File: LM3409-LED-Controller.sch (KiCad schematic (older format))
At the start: 24 parts, among them J1 PWM_IN, J2 IADJ, J3 BARREL_JACK, J4 LED+, J5 LED-, J6 EN, Q1 DMPH6050SK3, Q2 ZXMN7A11K, U1 LM3409HV-Q1

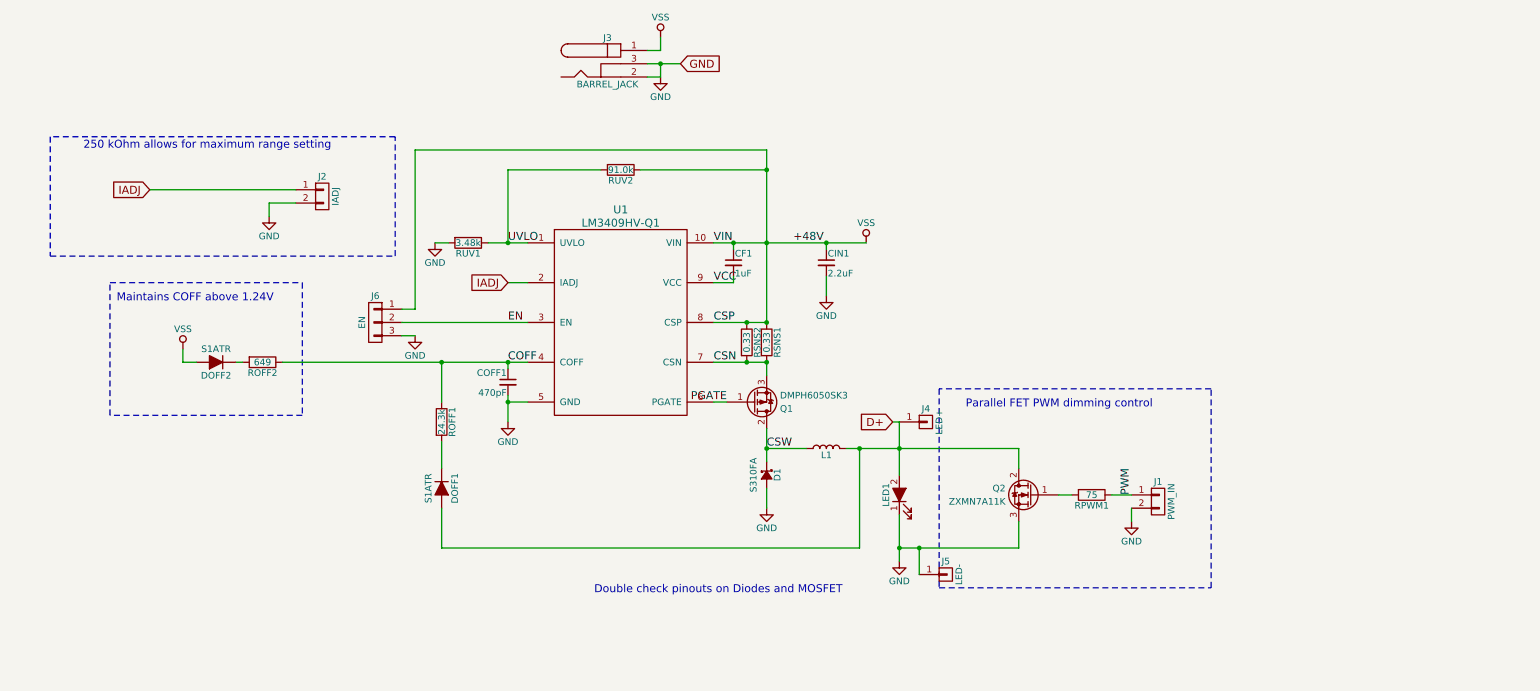
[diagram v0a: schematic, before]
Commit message: Replace parallel FET with CSD19538Q2 100-V, 49-mΩ NexFET. Added UCC27511 Gate Driver.
Redesign based on TI Designs: TIDA-01415.
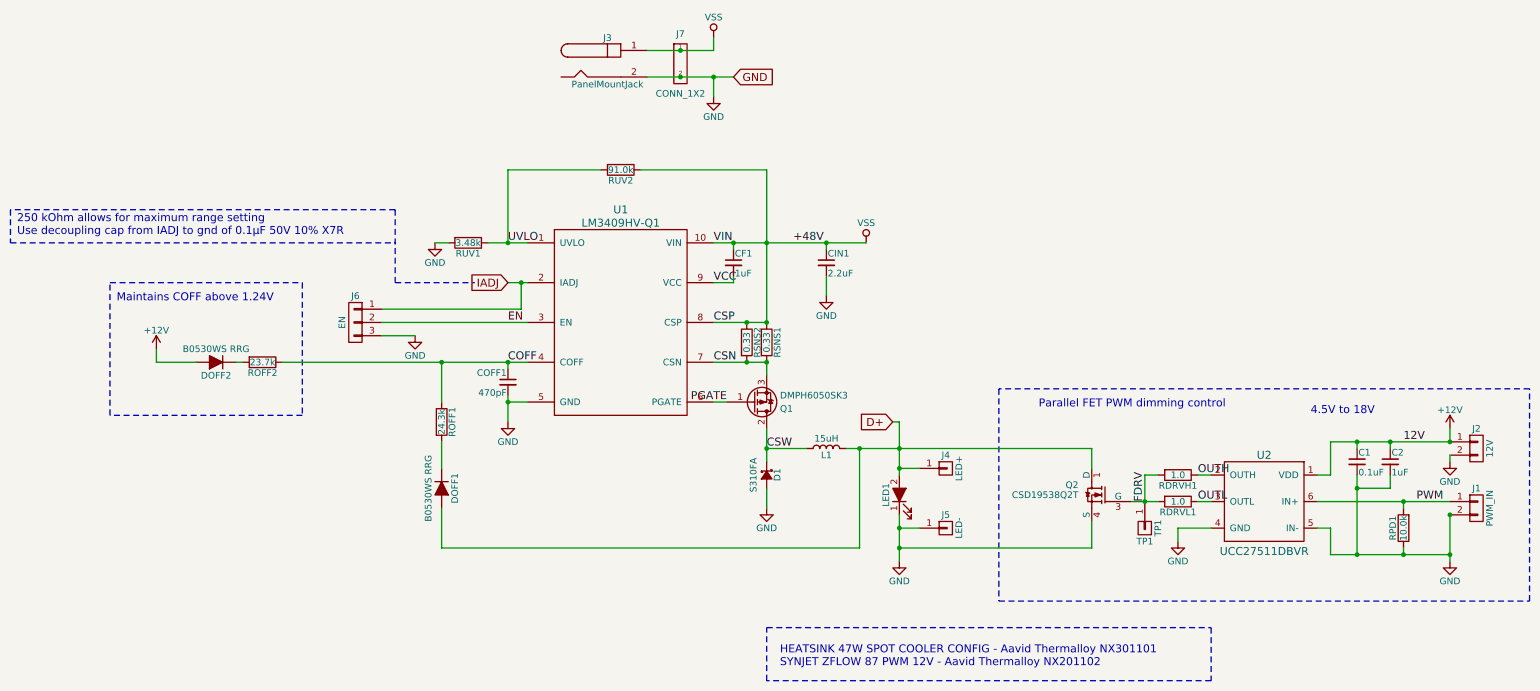
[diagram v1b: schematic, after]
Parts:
- removed J3: BARREL_JACK, Connectors:JACK_ALIM, symbol BARREL_JACK
- removed Q2: ZXMN7A11K, Project_Footprints:TO252_DPAK, symbol Q_NMOS_GDS
- removed RPWM1: 75, Resistors_SMD:R_0805, symbol R
- added C1: 0.1uF, Capacitors_SMD:C_0603, symbol C_Small
- added C2: 1uF, Capacitors_SMD:C_0805, symbol C_Small
- added J3: PanelMountJack, Project_Footprints:PanelMountJack_11mm, symbol PanelMountJack
- added J7: CONN_1X2, Wire_Connections_Bridges:WireConnection_2.00mmDrill, symbol CONN_1X2
- added Q2: CSD19538Q2T, Project_Footprints:SON_2mm_2mm_thermal, symbol CSD19538Q2T
- added RDRVH1, RDRVL1: 1.0, Resistors_SMD:R_0603, symbol R
- added RPD1: 10.0k, Resistors_SMD:R_0603, symbol R
- added TP1: TP1, Project_Footprints:Test_Point_1mm, symbol CONN_01X01
- added U2: UCC27511DBVR, Project_Footprints:SOT-23-1.75mm_3.0mm, symbol UCC27511DBVR
- CF1: footprint Capacitors_SMD:C_0603 -> Capacitors_SMD:C_0805; Description (none) -> CAP CER 1UF 50V X7R 0805
- CIN1: Description (none) -> CAP CER 2.2UF 100V X7R 1210; Part # (none) -> CL32B225KCJSNNE
- COFF1: Description (none) -> CAP CER 470PF 100V X7R 0402
- D1: Description (none) -> DIODE SCHOTTKY 100V 3A SOD123FA
- DOFF1, DOFF2: value S1ATR -> B0530WS RRG; footprint Project_Footprints:D_2026 -> Diodes_SMD:D_SOD-323F; Description (none) -> DIODE SCHOTTKY 30V 200MA SOD323F
- J2: value IADJ -> 12V
- L1: Description (none) -> FIXED IND 15UH 5A 27 MOHM SMD
- Q1: Description (none) -> MOSFET P-CH 60V 7.2A DPAK
- ROFF1: Description (none) -> RES SMD 24.3K OHM 1% 1/8W 0805
- ROFF2: value 649 -> 23.7k; Description (none) -> RES SMD 23.7K OHM 1% 1/8W 0805
- RSNS1, RSNS2: Description (none) -> RES 0.33 OHM 1% 1/2W 1206
- RUV1: Description (none) -> RES SMD 3.48K OHM 1% 1/8W 0805
- RUV2: Description (none) -> RES SMD 91K OHM 1% 1/8W 0805
- U1: Description (none) -> IC LED DRIVER CTRLR DIM 10MSOP
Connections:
- net D+: now also Q2.1 (D), Q2.2 (D), Q2.5 (D), Q2.6 (D), Q2.8 (D)
- net GND: now also C1.2, C2.2, J3.2, J7.2, Q2.4 (S), Q2.7 (S), RPD1.1, U2.4 (GND), U2.5 (IN-)
- net IADJ: now also J6.1 (P1); no longer J2.1 (P1)
- net PWM: now also RPD1.2, U2.6 (IN+)
- net VSS: now also J3.1, J7.1; no longer DOFF2.2 (A), J6.1 (P1)
- new net +12V: C1.1, C2.1, DOFF2.2 (A), J2.1 (P1), U2.1 (VDD)
- new net FDRV: Q2.3 (G), RDRVH1.2, RDRVL1.2, TP1.1 (P1)
- new net OUTH: RDRVH1.1, U2.2 (OUTH)
- new net OUTL: RDRVL1.1, U2.3 (OUTL)
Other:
- note added: "250 kOhm allows for maximum range setting\nUse decoupling cap from IADJ to gnd of 0.1µF 50V 10% X7R"
- note added: "4.5V to 18V"
- note added: "HEATSINK 47W SPOT COOLER CONFIG - Aavid Thermalloy NX301101\nSYNJET ZFLOW 87 PWM 12V - Aavid Thermalloy NX201102\n"
- note removed: "250 kOhm allows for maximum range setting"
- note removed: "Double check pinouts on Diodes and MOSFET"
- moved on the sheet: J1, J4, J5, J6

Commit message: Changed secondary voltage input to 9V
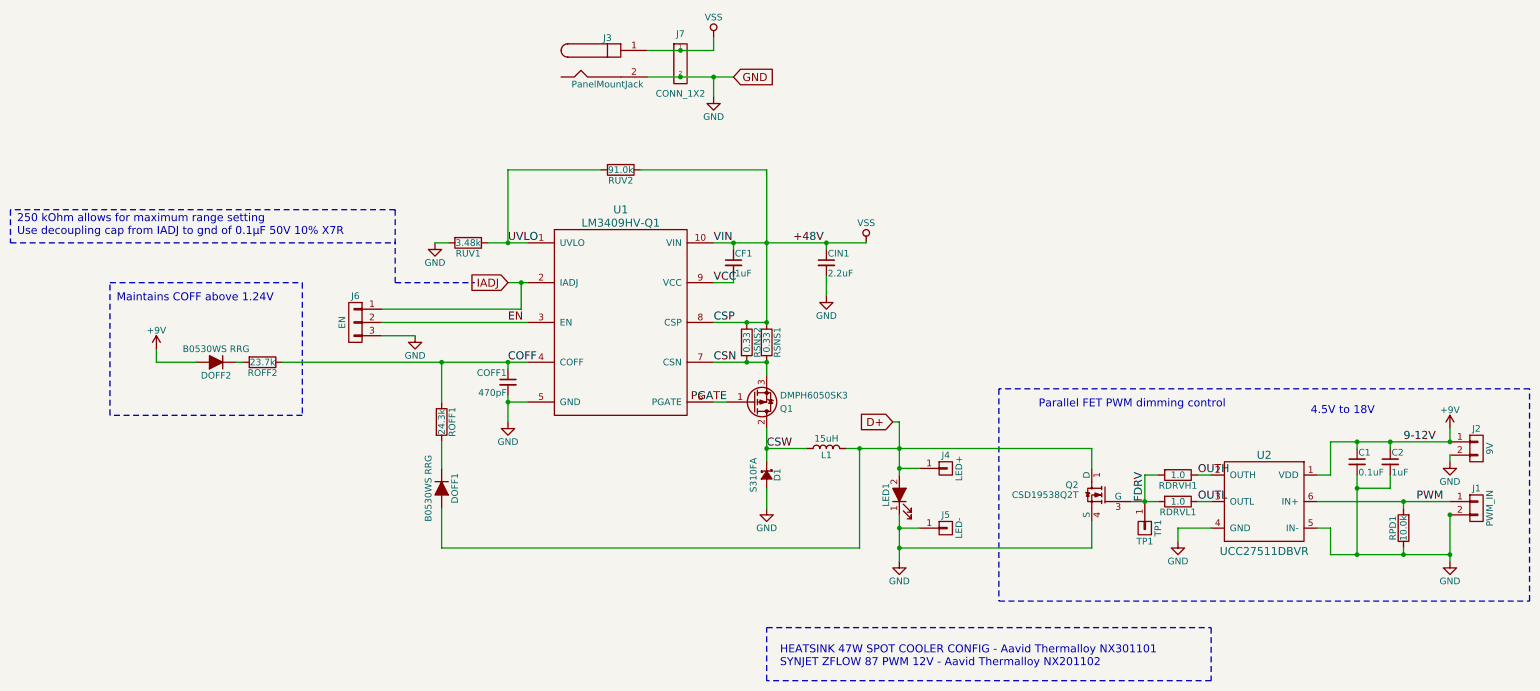
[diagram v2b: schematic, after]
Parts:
- J2: value 12V -> 9V
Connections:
- net +12V renamed +9V
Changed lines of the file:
@@
 	10650 5450 10650 5650
 Connection ~ 11200 5650
-$Comp
-L +12V #PWR012
-U 1 1 5A34D57E
-P 11550 4700
-F 0 "#PWR012" H 11550 4550 50  0001 C CNN
-F 1 "+12V" H 11550 4840 50  0000 C CNN
-F 2 "" H 11550 4700 50  0001 C CNN
-F 3 "" H 11550 4700 50  0001 C CNN
-	1    11550 4700
-	1    0    0    -1
-$EndComp
 Wire Wire Line
 	10650 4800 10850 4800
@@
 P 11750 4850
 F 0 "J2" H 11750 5000 50  0000 C CNN
-F 1 "12V" V 11850 4850 50  0000 C CNN
+F 1 "9V" V 11850 4850 50  0000 C CNN
 F 2 "Socket_Strips:Socket_Strip_Straight_1x02_Pitch2.54mm" H 11750 4850 50  0001 C CNN
 F 3 "" H 11750 4850 50  0001 C CNN
@@
 $EndComp
 Text Label 11200 4800 0    60   ~ 0
-12V
+9-12V
 Connection ~ 11550 5350
 Text Notes 10500 4600 0    60   ~ 0
@@
 Wire Wire Line
 	11550 4950 11550 4900
-$Comp
-L +12V #PWR014
-U 1 1 5A361223
-P 1800 4100
-F 0 "#PWR014" H 1800 3950 50  0001 C CNN
-F 1 "+12V" H 1800 4240 50  0000 C CNN
-F 2 "" H 1800 4100 50  0001 C CNN
-F 3 "" H 1800 4100 50  0001 C CNN
-	1    1800 4100
-	1    0    0    -1
-$EndComp
 Text Label 9650 5050 0    60   ~ 0
 OUTH
@@
 	0    1    1    0
 $EndComp
+$Comp
+L +9V #PWR?
+U 1 1 5A3CF371
+P 1800 4100
+F 0 "#PWR?" H 1800 3950 50  0001 C CNN
+F 1 "+9V" H 1800 4240 50  0000 C CNN
+F 2 "" H 1800 4100 50  0001 C CNN
+F 3 "" H 1800 4100 50  0001 C CNN
+	1    1800 4100
+	1    0    0    -1
+$EndComp
+$Comp
+L +9V #PWR?
+U 1 1 5A3CF844
+P 11550 4700
+F 0 "#PWR?" H 11550 4550 50  0001 C CNN
+F 1 "+9V" H 11550 4840 50  0000 C CNN
+F 2 "" H 11550 4700 50  0001 C CNN
+F 3 "" H 11550 4700 50  0001 C CNN
+	1    11550 4700
+	1    0    0    -1
+$EndComp
 $EndSCHEMATC

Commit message: Changes to LM3409 design
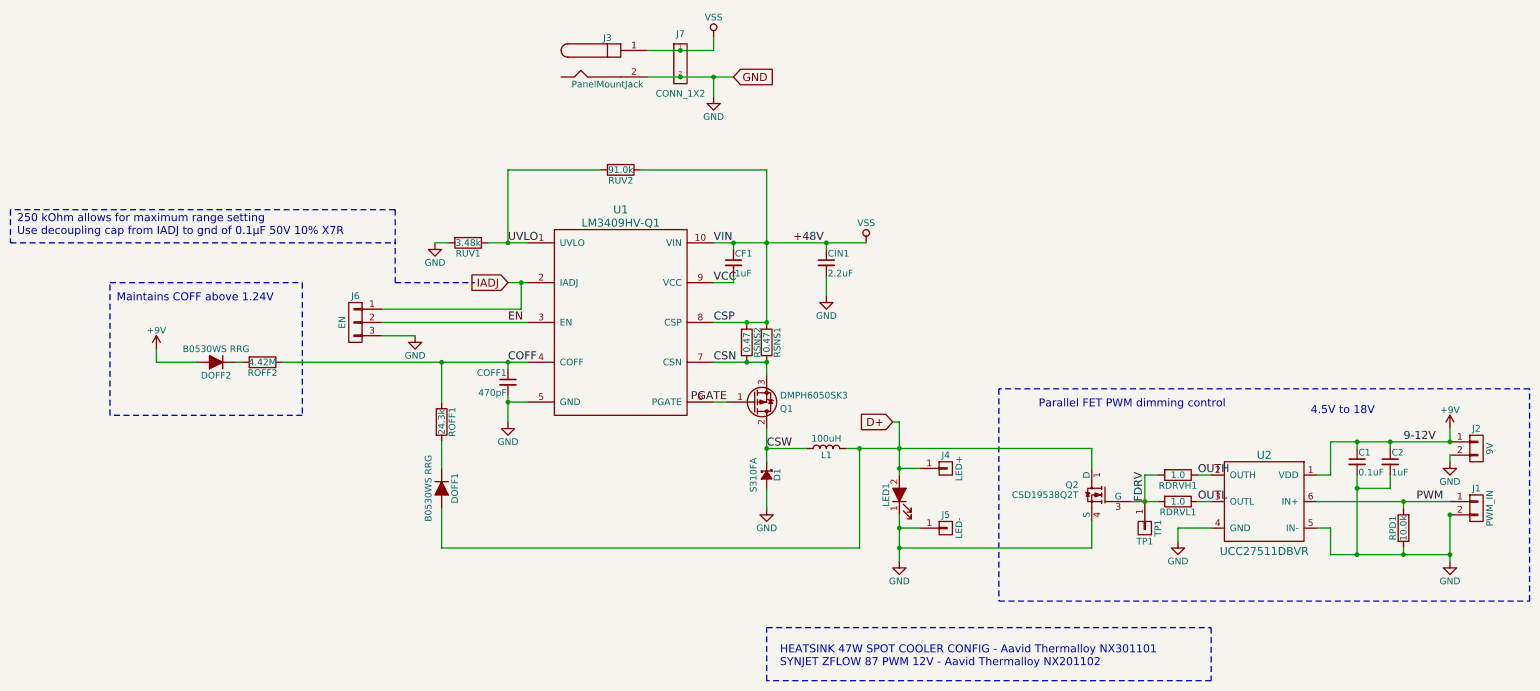
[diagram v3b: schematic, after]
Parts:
- L1: value 15uH -> 100uH; footprint Project_Footprints:L_SRR1260 -> Project_Footprints:L_SRR1280; Description FIXED IND 15UH 5A 27 MOHM SMD -> FIXED IND 100UH 2.1A 150 MOHM; Part SRR1260-150MCT-ND -> SRR1280-101M-ND
- ROFF2: value 23.7k -> 4.42M
- RSNS1, RSNS2: value 0.33 -> 0.47; Description RES 0.33 OHM 1% 1/2W 1206 -> RES 0.47 OHM 1% 1/2W 1206; Part # (none) -> ERJ-8BQFR47V
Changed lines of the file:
@@
 P 6400 4050
 F 0 "RSNS1" V 6480 4050 50  0000 C CNN
-F 1 "0.33" V 6400 4050 50  0000 C CNN
+F 1 "0.47" V 6400 4050 50  0000 C CNN
 F 2 "Resistors_SMD:R_1206" V 6330 4050 50  0001 C CNN
 F 3 "" H 6400 4050 50  0001 C CNN
-F 4 "RES 0.33 OHM 1% 1/2W 1206" V 6400 4050 60  0001 C CNN "Description"
+F 4 "RES 0.47 OHM 1% 1/2W 1206" V 6400 4050 60  0001 C CNN "Description"
+F 5 "ERJ-8BQFR47V" V 6400 4050 60  0001 C CNN "Part #"
 	1    6400 4050
 	1    0    0    -1
@@
 $EndComp
 Wire Wire Line
-	6400 3900 6250 3900
-Wire Wire Line
-	6250 3900 6000 3900
-Wire Wire Line
-	6000 4200 6250 4200
-Wire Wire Line
-	6250 4200 6400 4200
-Wire Wire Line
-	4300 3300 4450 3300
-Wire Wire Line
-	4450 3300 4600 3300
+	6400 3900 6000 3900
+Wire Wire Line
+	6000 4200 6400 4200
+Wire Wire Line
+	4300 3300 4600 3300
 Wire Wire Line
 	5150 2750 4450 2750
@@
 	5450 2750 6400 2750
 Wire Wire Line
-	6000 3300 6150 3300
-Wire Wire Line
-	6150 3300 6400 3300
-Wire Wire Line
-	6400 3300 6850 3300
-Wire Wire Line
-	6850 3300 7150 3300
-$Comp
-L GND #PWR01
+	6000 3300 7150 3300
+$Comp
+L GND #PWR3
 U 1 1 5A1E24A2
 P 3900 3300
-F 0 "#PWR01" H 3900 3050 50  0001 C CNN
+F 0 "#PWR3" H 3900 3050 50  0001 C CNN
 F 1 "GND" H 3900 3150 50  0000 C CNN
 F 2 "" H 3900 3300 50  0001 C CNN
@@
 Connection ~ 4450 4200
 Wire Wire Line
-	4450 4450 4450 4500
-Wire Wire Line
-	4450 4500 4450 4650
+	4450 4450 4450 4650
 Wire Wire Line
 	4450 4500 4600 4500
@@
 	6400 4200 6400 4300
 Wire Wire Line
-	6400 4700 6400 4850
-Wire Wire Line
-	6400 4850 6400 4950
-$Comp
-L GND #PWR02
+	6400 4700 6400 4950
+$Comp
+L GND #PWR7
 U 1 1 5A1E2EDD
 P 6400 5300
-F 0 "#PWR02" H 6400 5050 50  0001 C CNN
+F 0 "#PWR7" H 6400 5050 50  0001 C CNN
 F 1 "GND" H 6400 5150 50  0000 C CNN
 F 2 "" H 6400 5300 50  0001 C CNN
@@
 P 6850 4850
 F 0 "L1" V 6800 4850 50  0000 C CNN
-F 1 "15uH" V 6925 4850 50  0000 C CNN
-F 2 "Project_Footprints:L_SRR1260" H 6850 4850 50  0001 C CNN
-F 3 "http://www.bourns.com/docs/Product-Datasheets/SRR1260.pdf" H 6850 4850 50  0001 C CNN
-F 4 "SRR1260-150MCT-ND" V 6850 4850 60  0001 C CNN "Part"
-F 5 "FIXED IND 15UH 5A 27 MOHM SMD" V 6850 4850 60  0001 C CNN "Description"
+F 1 "100uH" V 6925 4850 50  0000 C CNN
+F 2 "Project_Footprints:L_SRR1280" H 6850 4850 50  0001 C CNN
+F 3 "http://www.bourns.com/docs/Product-Datasheets/SRR1280.pdf" H 6850 4850 50  0001 C CNN
+F 4 "SRR1280-101M-ND" V 6850 4850 60  0001 C CNN "Part"
+F 5 "FIXED IND 100UH 2.1A 150 MOHM" V 6850 4850 60  0001 C CNN "Description"
 	1    6850 4850
 	0    -1   -1   0
@@
 Connection ~ 6400 4850
 Wire Wire Line
-	7000 4850 7100 4850
-Wire Wire Line
-	7100 4850 7400 4850
-Wire Wire Line
-	7400 4850 8850 4850
+	7000 4850 8850 4850
 Wire Wire Line
 	7100 4850 7100 5600
@@
 	7100 5600 3950 5600
 Wire Wire Line
-	7400 4650 7400 4850
-Wire Wire Line
-	7400 4850 7400 5000
-Wire Wire Line
-	7400 5000 7400 5050
+	7400 4650 7400 5050
 Connection ~ 7100 4850
 $Comp
@@
 Connection ~ 6400 3300
 Wire Wire Line
-	6400 2750 6400 3300
-Wire Wire Line
-	6400 3300 6400 3900
+	6400 2750 6400 3900
 Connection ~ 6400 3900
 $Comp
-L VSS #PWR03
+L VSS #PWR9
 U 1 1 5A1E3B57
 P 7150 3300
-F 0 "#PWR03" H 7150 3150 50  0001 C CNN
+F 0 "#PWR9" H 7150 3150 50  0001 C CNN
 F 1 "VSS" H 7150 3450 50  0000 C CNN
 F 2 "" H 7150 3300 50  0001 C CNN
@@
 Connection ~ 6850 3300
 $Comp
-L GND #PWR04
+L GND #PWR8
 U 1 1 5A1E3BD3
 P 6850 3700
-F 0 "#PWR04" H 6850 3450 50  0001 C CNN
+F 0 "#PWR8" H 6850 3450 50  0001 C CNN
 F 1 "GND" H 6850 3550 50  0000 C CNN
 F 2 "" H 6850 3700 50  0001 C CNN
@@
 	8850 5600 8850 5400
 $Comp
-L GND #PWR05
+L GND #PWR10
 U 1 1 5A1E4017
 P 7400 5700
-F 0 "#PWR05" H 7400 5450 50  0001 C CNN
+F 0 "#PWR10" H 7400 5450 50  0001 C CNN
 F 1 "GND" H 7400 5550 50  0000 C CNN
 F 2 "" H 7400 5700 50  0001 C CNN
@@
 $EndComp
 Wire Wire Line
-	7400 5350 7400 5450
-Wire Wire Line
-	7400 5450 7400 5600
-Wire Wire Line
-	7400 5600 7400 5700
+	7400 5350 7400 5700
 Wire Wire Line
 	7400 5600 8850 5600
 Connection ~ 7400 5600
 Wire Wire Line
-	2750 4200 3950 4200
-Wire Wire Line
-	3950 4200 4450 4200
-Wire Wire Line
-	4450 4200 4600 4200
+	2750 4200 4600 4200
 $Comp
 L R ROFF2
@@
 P 2600 4200
 F 0 "ROFF2" V 2680 4200 50  0000 C CNN
-F 1 "23.7k" V 2600 4200 50  0000 C CNN
+F 1 "4.42M" V 2600 4200 50  0000 C CNN
 F 2 "Resistors_SMD:R_0805" V 2530 4200 50  0001 C CNN
 F 3 "http://www.vishay.com/docs/20035/dcrcwe3.pdf" H 2600 4200 50  0001 C CNN
@@
 IADJ
 Wire Wire Line
-	4450 3600 4550 3600
-Wire Wire Line
-	4550 3600 4600 3600
-$Comp
-L R RSNS2
-U 1 1 5A229AA6
-P 6250 4050
-F 0 "RSNS2" V 6330 4050 50  0000 C CNN
-F 1 "0.33" V 6250 4050 50  0000 C CNN
-F 2 "Resistors_SMD:R_1206" V 6180 4050 50  0001 C CNN
-F 3 "" H 6250 4050 50  0001 C CNN
-F 4 "RES 0.33 OHM 1% 1/2W 1206" V 6250 4050 60  0001 C CNN "Description"
-	1    6250 4050
-	1    0    0    -1
-$EndComp
+	4450 3600 4600 3600
 Connection ~ 6250 3900
 Connection ~ 6250 4200
@@
 $EndComp
 $Comp
-L GND #PWR06
+L GND #PWR14
 U 1 1 5A22D4FE
 P 11550 5700
-F 0 "#PWR06" H 11550 5450 50  0001 C CNN
+F 0 "#PWR14" H 11550 5450 50  0001 C CNN
 F 1 "GND" H 11550 5550 50  0000 C CNN
 F 2 "" H 11550 5700 50  0001 C CNN
@@
 $EndComp
 Wire Wire Line
-	11550 5350 11550 5650
-Wire Wire Line
-	11550 5650 11550 5700
-$Comp
-L VSS #PWR07
+	11550 5350 11550 5700
+$Comp
+L VSS #PWR5
 U 1 1 5A230C84
 P 6000 1750
-F 0 "#PWR07" H 6000 1600 50  0001 C CNN
+F 0 "#PWR5" H 6000 1600 50  0001 C CNN
 F 1 "VSS" H 6000 1900 50  0000 C CNN
 F 2 "" H 6000 1750 50  0001 C CNN
@@
 	6000 1850 6000 1750
 Wire Wire Line
-	5500 1850 5750 1850
-Wire Wire Line
-	5750 1850 6000 1850
-$Comp
-L GND #PWR08
+	5500 1850 6000 1850
+$Comp
+L GND #PWR6
 U 1 1 5A230D2C
 P 6000 2200
-F 0 "#PWR08" H 6000 1950 50  0001 C CNN
+F 0 "#PWR6" H 6000 1950 50  0001 C CNN
 F 1 "GND" H 6000 2050 50  0000 C CNN
 F 2 "" H 6000 2200 50  0001 C CNN
@@
 CSP
 $Comp
-L GND #PWR09
+L GND #PWR4
 U 1 1 5A25FAA1
 P 4450 4650
-F 0 "#PWR09" H 4450 4400 50  0001 C CNN
+F 0 "#PWR4" H 4450 4400 50  0001 C CNN
 F 1 "GND" H 4450 4500 50  0000 C CNN
 F 2 "" H 4450 4650 50  0001 C CNN
@@
 $EndComp
 $Comp
-L GND #PWR010
+L GND #PWR2
 U 1 1 5A2A16EA
 P 3750 4000
-F 0 "#PWR010" H 3750 3750 50  0001 C CNN
+F 0 "#PWR2" H 3750 3750 50  0001 C CNN
 F 1 "GND" H 3750 3850 50  0000 C CNN
 F 2 "" H 3750 4000 50  0001 C CNN
@@
 CSW
 Wire Wire Line
-	10550 5250 11200 5250
-Wire Wire Line
-	11200 5250 11550 5250
-Wire Wire Line
-	5500 2050 5750 2050
-Wire Wire Line
-	5750 2050 6000 2050
-Wire Wire Line
-	6000 2050 6150 2050
+	10550 5250 11550 5250
+Wire Wire Line
+	5500 2050 6150 2050
 $Comp
 L PanelMountJack J3
@@
 $EndComp
 Wire Wire Line
-	9150 5250 9250 5250
-Wire Wire Line
-	9250 5250 9350 5250
+	9150 5250 9350 5250
 Wire Wire Line
 	9350 5050 9250 5050
@@
 	9750 5250 9650 5250
 $Comp
-L GND #PWR011
+L GND #PWR11
 U 1 1 5A34BC8B
 P 9500 5550
-F 0 "#PWR011" H 9500 5300 50  0001 C CNN
+F 0 "#PWR11" H 9500 5300 50  0001 C CNN
 F 1 "GND" H 9500 5400 50  0000 C CNN
 F 2 "" H 9500 5550 50  0001 C CNN
@@
 	11200 5650 11200 5600
 Wire Wire Line
-	10650 5650 10850 5650
-Wire Wire Line
-	10850 5650 11200 5650
-Wire Wire Line
-	11200 5650 11550 5650
+	10650 5650 11550 5650
 Connection ~ 11550 5650
 Connection ~ 11200 5250
@@
 Connection ~ 11200 5650
 Wire Wire Line
-	10650 4800 10850 4800
-Wire Wire Line
-	10850 4800 11100 4800
-Wire Wire Line
-	11100 4800 11550 4800
+	10650 4800 11550 4800
 Wire Wire Line
 	10650 4800 10650 5050
@@
 $EndComp
 Wire Wire Line
-	10850 5050 10850 5150
-Wire Wire Line
-	10850 5150 10850 5650
+	10850 5050 10850 5650
 Connection ~ 10850 5650
 Wire Wire Line
@@
 Connection ~ 11550 4800
 $Comp
-L GND #PWR013
+L GND #PWR13
 U 1 1 5A360057
 P 11550 4950
-F 0 "#PWR013" H 11550 4700 50  0001 C CNN
+F 0 "#PWR13" H 11550 4700 50  0001 C CNN
 F 1 "GND" H 11550 4800 50  0000 C CNN
 F 2 "" H 11550 4950 50  0001 C CNN
@@
 $EndComp
 $Comp
-L +9V #PWR?
+L +9V #PWR1
 U 1 1 5A3CF371
 P 1800 4100
-F 0 "#PWR?" H 1800 3950 50  0001 C CNN
+F 0 "#PWR1" H 1800 3950 50  0001 C CNN
 F 1 "+9V" H 1800 4240 50  0000 C CNN
 F 2 "" H 1800 4100 50  0001 C CNN
@@
 $EndComp
 $Comp
-L +9V #PWR?
+L +9V #PWR12
 U 1 1 5A3CF844
 P 11550 4700
-F 0 "#PWR?" H 11550 4550 50  0001 C CNN
+F 0 "#PWR12" H 11550 4550 50  0001 C CNN
 F 1 "+9V" H 11550 4840 50  0000 C CNN
 F 2 "" H 11550 4700 50  0001 C CNN
@@
 	1    0    0    -1
 $EndComp
+$Comp
+L R RSNS2
+U 1 1 5A505C64
+P 6250 4050
+F 0 "RSNS2" V 6330 4050 50  0000 C CNN
+F 1 "0.47" V 6250 4050 50  0000 C CNN
+F 2 "Resistors_SMD:R_1206" V 6180 4050 50  0001 C CNN
+F 3 "" H 6250 4050 50  0001 C CNN
+F 4 "RES 0.47 OHM 1% 1/2W 1206" V 6250 4050 60  0001 C CNN "Description"
+F 5 "ERJ-8BQFR47V" V 6250 4050 60  0001 C CNN "Part #"
+	1    6250 4050
+	1    0    0    -1
+$EndComp
